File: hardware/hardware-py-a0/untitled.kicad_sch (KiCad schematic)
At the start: 25 parts, among them J12 Micro_SD_Card_Det2, J4 LCD_socket, J9 AudioJack4, Q8 BSS138, Q9 BSS138

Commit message: [dev] py-a0 board files
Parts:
- removed R13: 10k, Resistor_SMD:R_0805_2012Metric_Pad1.20x1.40mm_HandSolder, symbol Device:R
- R27: value 10k -> 1M
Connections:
- net BUZZER: now also Q8.1 (G), R27.1
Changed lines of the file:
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@@
+	)
+	(junction
+		(at 128.27 176.53)
+		(diameter 0)
+		(color 0 0 0 0)
 	)
 	(junction
@@
 	)
 	(junction
-		(at 128.27 176.53)
-		(diameter 0)
-		(color 0 0 0 0)
-	)
-	(junction
 		(at 91.44 67.31)
 		(diameter 0)
@@
 	(wire
 		(pts
+			(xy 128.27 176.53) (xy 158.75 176.53)
+		)
+		(stroke
+			(width 0)
+			(type default)
+		)
+	)
+	(wire
+		(pts
 			(xy 144.78 54.61) (xy 147.32 54.61)
 		)
@@
 		(pts
 			(xy 165.1 67.31) (xy 149.86 67.31)
-		)
-		(stroke
-			(width 0)
-			(type default)
-		)
-	)
-	(wire
-		(pts
-			(xy 135.89 176.53) (xy 158.75 176.53)
 		)
 		(stroke
@@
 			)
 		)
-		(property "Value" "10k"
+		(property "Value" "1M"
 			(at 125.476 180.848 90)
 			(effects
@@
 					(unit 1)
 				)
-			)
-		)
-	)
-	(symbol
-		(lib_id "Device:R")
-		(at 132.08 176.53 270)
-		(mirror x)
-		(unit 1)
-		(exclude_from_sim no)
-		(in_bom yes)
-		(on_board yes)
-		(dnp no)
-		(property "Reference" "R13"
-			(at 131.572 179.324 90)
-			(effects
-				(font
-					(size 1.27 1.27)
-				)
-			)
-		)
-		(property "Value" "10k"
-			(at 131.572 173.736 90)
-			(effects
-				(font
-					(size 1.27 1.27)
-				)
-			)
-		)
-		(property "Footprint" "Resistor_SMD:R_0805_2012Metric_Pad1.20x1.40mm_HandSolder"
-			(at 132.08 178.308 90)
-			(effects
-				(font
-					(size 1.27 1.27)
-				)
-				(hide yes)
-			)
-		)
-		(property "Datasheet" "~"
-			(at 132.08 176.53 0)
-			(effects
-				(font
-					(size 1.27 1.27)
-				)
-				(hide yes)
-			)
-		)
-		(property "Description" "Resistor"
-			(at 132.08 176.53 0)
-			(effects
-				(font
-					(size 1.27 1.27)
-				)
-				(hide yes)
-			)
-		)
-		(pin "1"
-		)
-		(pin "2"
-		)
-		(instances
-			(project "numcalcium"
-				(path "/842c0813-91d3-4f68-bc1f-ac3ce07be478/88d65574-4a55-44b9-b6d2-8e7d5a1c096b"
-					(reference "R13")
-					(unit 1)
-				)

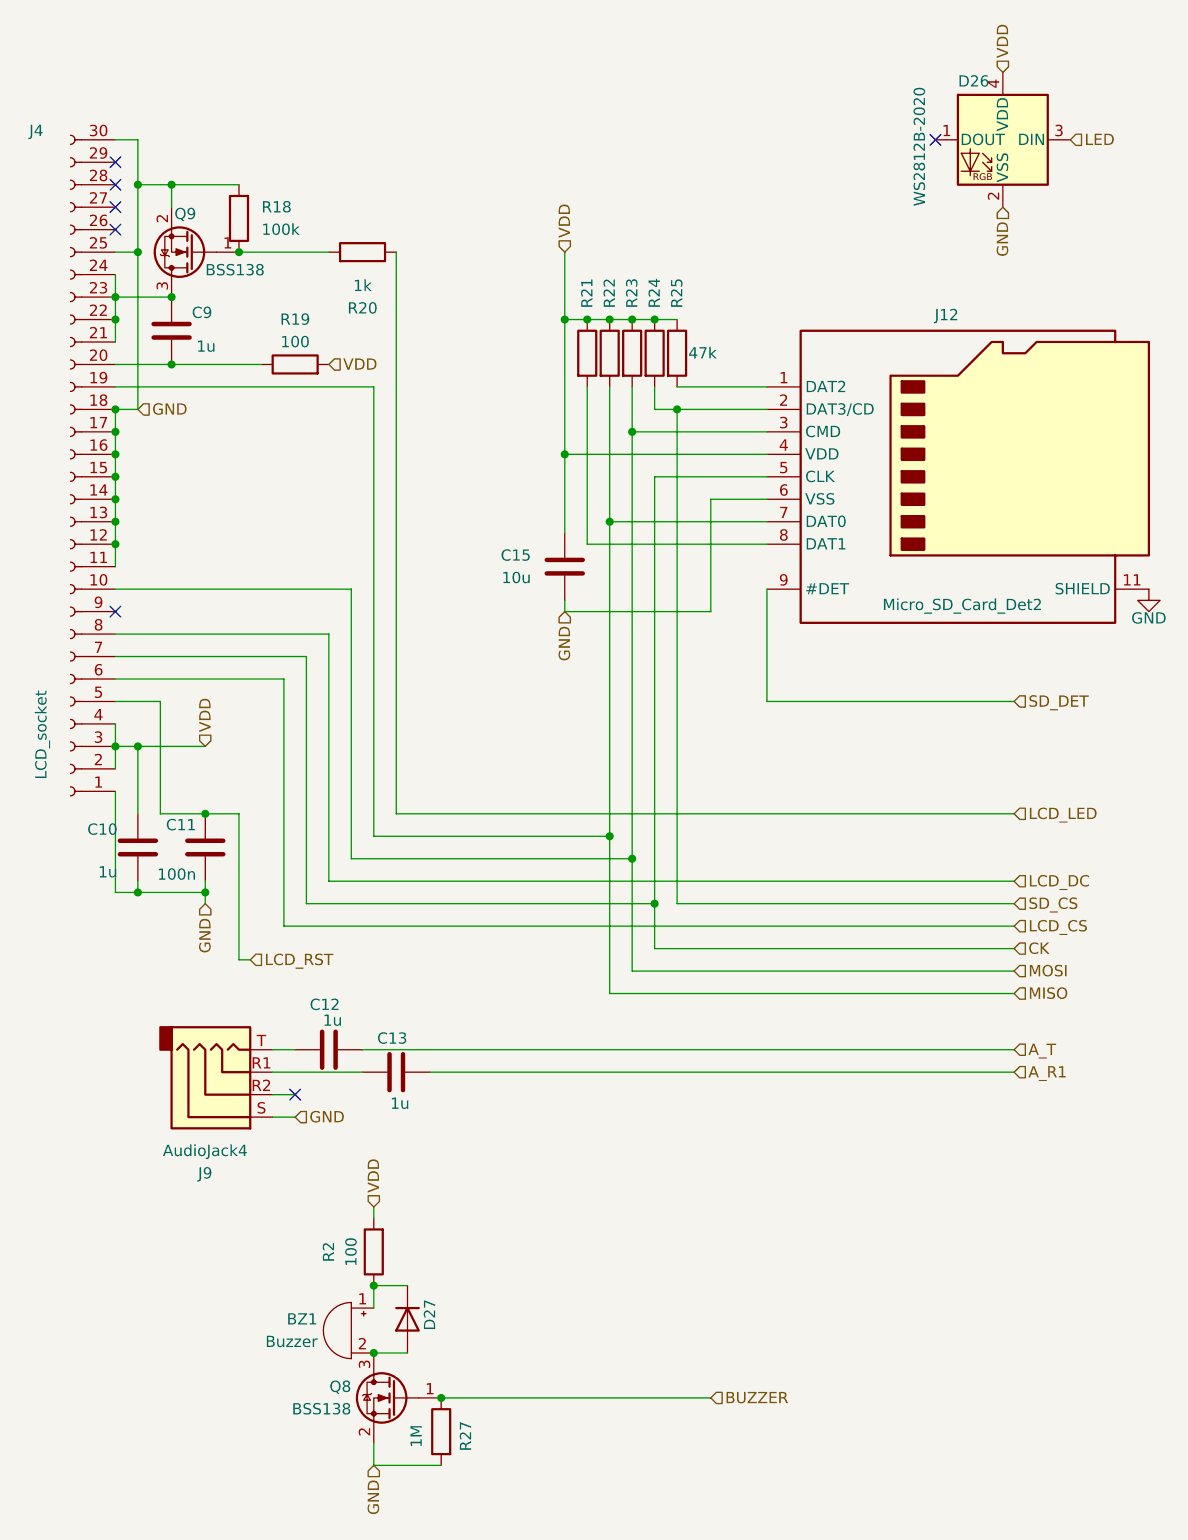
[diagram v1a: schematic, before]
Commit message: hardware: py/a0 revision 1.1 using FFC connectors
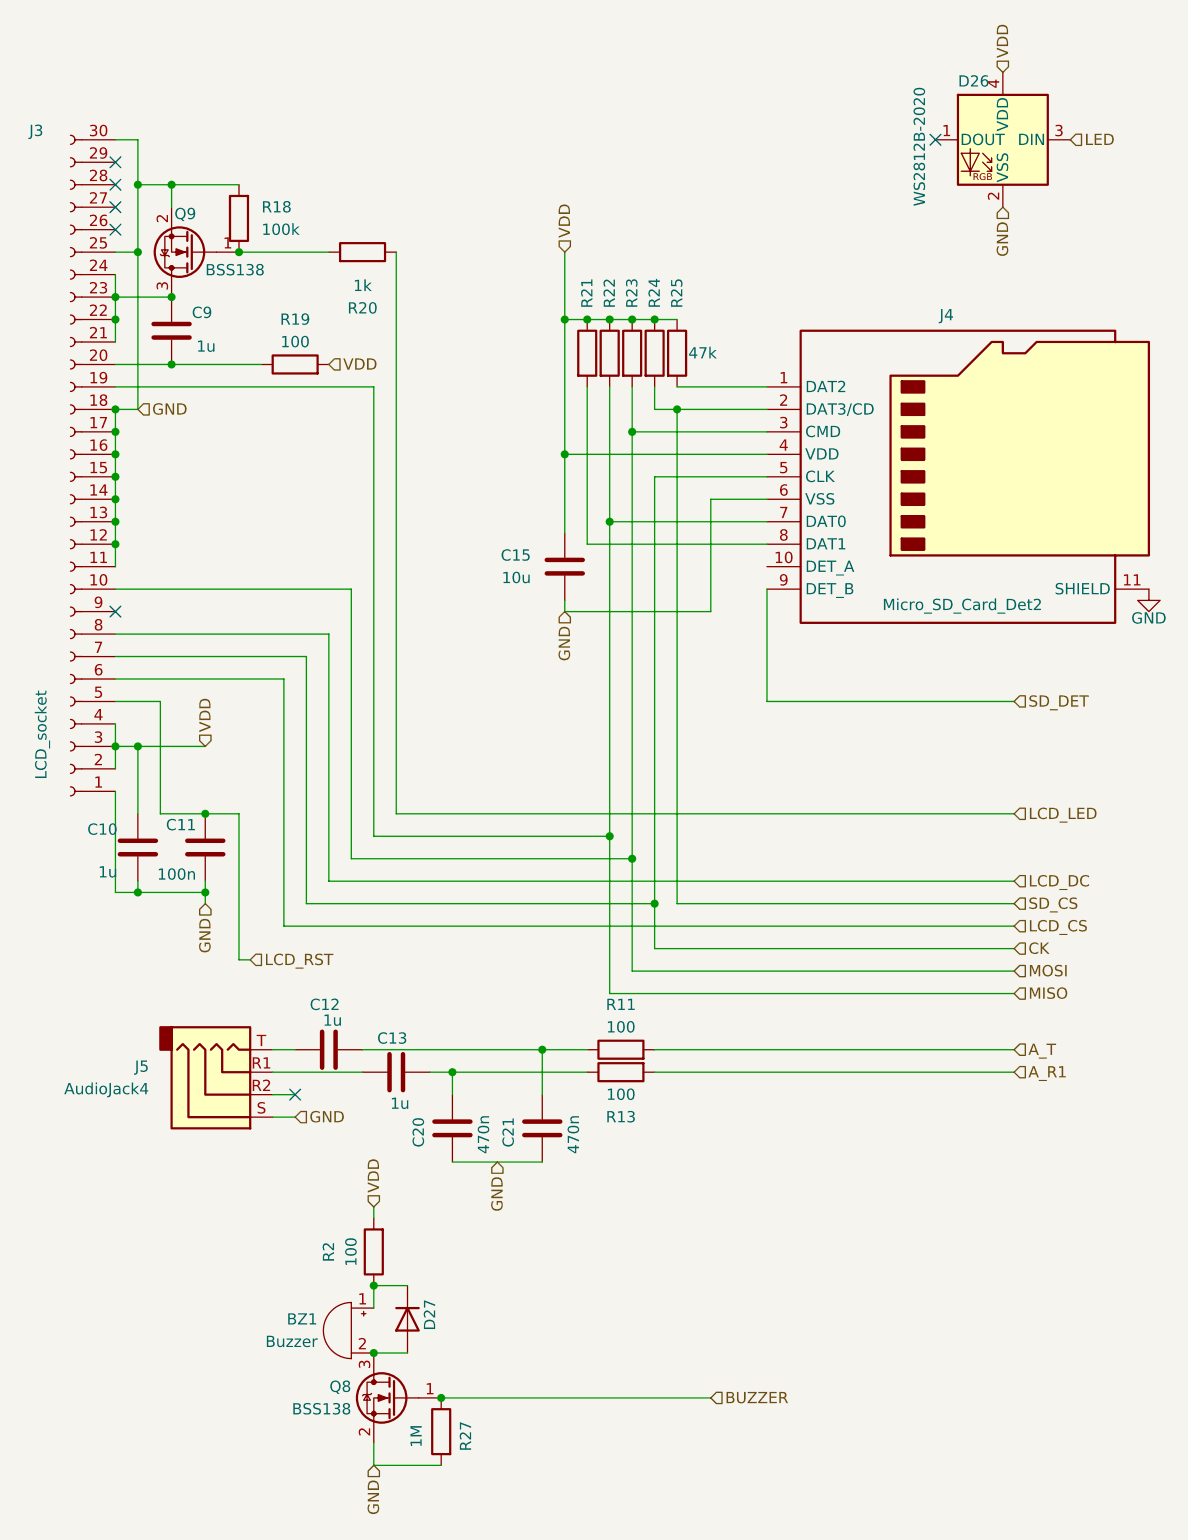
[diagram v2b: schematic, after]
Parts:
- added C20, C21: 470n, Capacitor_SMD:C_0805_2012Metric, symbol Device:C
- added R11, R13: 100, Resistor_SMD:R_0805_2012Metric_Pad1.20x1.40mm_HandSolder, symbol Device:R
- D27: footprint Diode_SMD:D_0805_2012Metric_Pad1.15x1.40mm_HandSolder -> Diode_SMD:D_1206_3216Metric
- renumbered J4 to J3, J12 to J4, J9 to J5
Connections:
- net A_R1: now also R13.2; no longer C13.2
- net A_T: now also R11.2; no longer C12.2
- net GND: now also C20.1, C21.1
- new net: C13.2, C20.2, R13.1
- new net: C12.2, C21.2, R11.1
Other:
- company, title: (none) -> MOTIV.PW

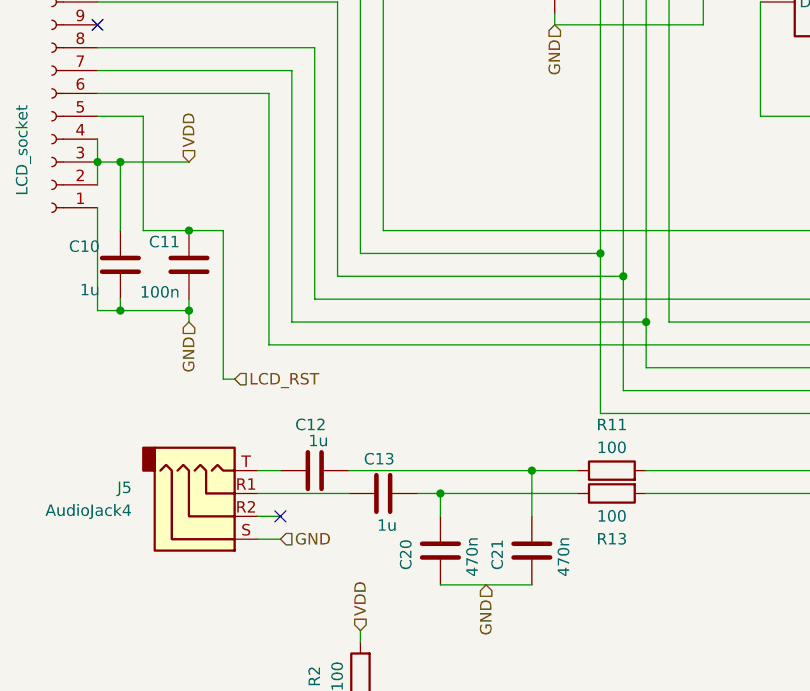
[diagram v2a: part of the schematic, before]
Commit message: terminal:os.dupterm Stream support
move files and rename folders to board_src and scripts
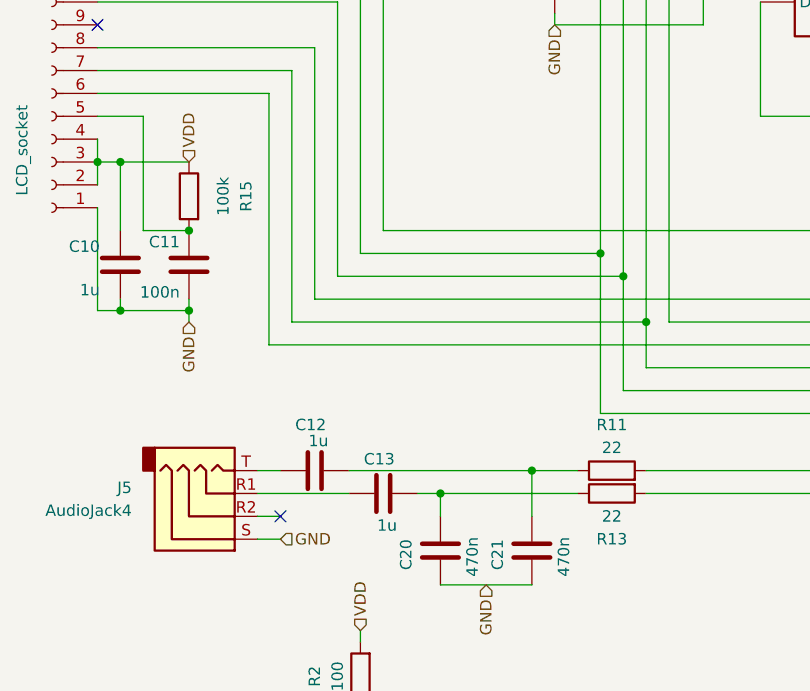
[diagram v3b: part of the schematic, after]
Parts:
- added R15: 100k, Resistor_SMD:R_0805_2012Metric_Pad1.20x1.40mm_HandSolder, symbol Device:R
- R11, R13: value 100 -> 22
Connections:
- net VDD: now also R15.1
- net LCD_RST: no longer names the net of C11.1, J3.5 (Pin_5)
- net LCD_RST: now also R15.2
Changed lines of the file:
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@@
+	)
+	(junction
+		(at 91.44 64.77)
+		(diameter 0)
+		(color 0 0 0 0)
+	)
+	(junction
+		(at 91.44 52.07)
+		(diameter 0)
+		(color 0 0 0 0)
+	)
+	(junction
+		(at 91.44 69.85)
+		(diameter 0)
+		(color 0 0 0 0)
+	)
+	(junction
+		(at 149.86 67.31)
+		(diameter 0)
+		(color 0 0 0 0)
+	)
+	(junction
+		(at 91.44 67.31)
+		(diameter 0)
+		(color 0 0 0 0)
+	)
+	(junction
+		(at 142.24 54.61)
+		(diameter 0)
+		(color 0 0 0 0)
+	)
+	(junction
+		(at 93.98 46.99)
+		(diameter 0)
+		(color 0 0 0 0)
+	)
+	(junction
+		(at 97.79 52.07)
+		(diameter 0)
+		(color 0 0 0 0)
+	)
+	(junction
+		(at 152.4 54.61)
+		(diameter 0)
+		(color 0 0 0 0)
+	)
+	(junction
+		(at 147.32 77.47)
+		(diameter 0)
+		(color 0 0 0 0)
+	)
+	(junction
+		(at 149.86 115.57)
+		(diameter 0)
+		(color 0 0 0 0)
+	)
+	(junction
+		(at 142.24 69.85)
+		(diameter 0)
+		(color 0 0 0 0)
+	)
+	(junction
+		(at 91.44 77.47)
+		(diameter 0)
+		(color 0 0 0 0)
 	)
 	(junction
@@
 	)
 	(junction
-		(at 91.44 64.77)
-		(diameter 0)
-		(color 0 0 0 0)
-	)
-	(junction
-		(at 91.44 52.07)
-		(diameter 0)
-		(color 0 0 0 0)
-	)
-	(junction
-		(at 91.44 69.85)
-		(diameter 0)
-		(color 0 0 0 0)
-	)
-	(junction
-		(at 149.86 67.31)
-		(diameter 0)
-		(color 0 0 0 0)
-	)
-	(junction
-		(at 91.44 67.31)
-		(diameter 0)
-		(color 0 0 0 0)
-	)
-	(junction
-		(at 142.24 54.61)
-		(diameter 0)
-		(color 0 0 0 0)
-	)
-	(junction
-		(at 93.98 46.99)
-		(diameter 0)
-		(color 0 0 0 0)
-	)
-	(junction
-		(at 97.79 52.07)
-		(diameter 0)
-		(color 0 0 0 0)
-	)
-	(junction
-		(at 152.4 54.61)
-		(diameter 0)
-		(color 0 0 0 0)
-	)
-	(junction
-		(at 147.32 77.47)
-		(diameter 0)
-		(color 0 0 0 0)
-	)
-	(junction
-		(at 149.86 115.57)
-		(diameter 0)
-		(color 0 0 0 0)
-	)
-	(junction
-		(at 142.24 69.85)
-		(diameter 0)
-		(color 0 0 0 0)
-	)
-	(junction
-		(at 91.44 77.47)
-		(diameter 0)
-		(color 0 0 0 0)
-	)
-	(junction
 		(at 129.54 139.7)
 		(diameter 0)
@@
 	(wire
 		(pts
-			(xy 105.41 110.49) (xy 101.6 110.49)
-		)
-		(stroke
-			(width 0)
-			(type default)
-		)
-	)
-	(wire
-		(pts
-			(xy 105.41 127) (xy 105.41 110.49)
-		)
-		(stroke
-			(width 0)
-			(type default)
-		)
-	)
-	(wire
-		(pts
 			(xy 120.65 154.94) (xy 120.65 156.21)
 		)
@@
 	(wire
 		(pts
-			(xy 105.41 127) (xy 106.68 127)
-		)
-		(stroke
-			(width 0)
-			(type default)
-		)
-	)
-	(wire
-		(pts
 			(xy 149.86 67.31) (xy 149.86 62.23)
 		)
@@
 		(shape input)
 		(at 111.76 144.78 0)
-		(fields_autoplaced yes)
-		(effects
-			(font
-				(size 1.27 1.27)
-			)
-			(justify left)
-		)
-	)
-	(hierarchical_label "LCD_RST"
-		(shape input)
-		(at 106.68 127 0)
 		(fields_autoplaced yes)
 		(effects
@@
 				(path "/842c0813-91d3-4f68-bc1f-ac3ce07be478/88d65574-4a55-44b9-b6d2-8e7d5a1c096b"
 					(reference "R22")
+					(unit 1)
+				)
+			)
+		)
+	)
+	(symbol
+		(lib_id "Device:R")
+		(at 101.6 106.68 0)
+		(mirror y)
+		(unit 1)
+		(exclude_from_sim no)
+		(in_bom yes)
+		(on_board yes)
+		(dnp no)
+		(property "Reference" "R15"
+			(at 107.95 106.68 90)
+			(effects
+				(font
+					(size 1.27 1.27)
+				)
+			)
+		)
+		(property "Value" "100k"
+			(at 105.41 106.68 90)
+			(effects
+				(font
+					(size 1.27 1.27)
+				)
+			)
+		)
+		(property "Footprint" "Resistor_SMD:R_0805_2012Metric_Pad1.20x1.40mm_HandSolder"
+			(at 103.378 106.68 90)
+			(effects
+				(font
+					(size 1.27 1.27)
+				)
+				(hide yes)
+			)
+		)
+		(property "Datasheet" "~"
+			(at 101.6 106.68 0)
+			(effects
+				(font
+					(size 1.27 1.27)
+				)
+				(hide yes)
+			)
+		)
+		(property "Description" "Resistor"
+			(at 101.6 106.68 0)
+			(effects
+				(font
+					(size 1.27 1.27)
+				)
+				(hide yes)
+			)
+		)
+		(pin "1"
+		)
+		(pin "2"
+		)
+		(instances
+			(project "numcalcium"
+				(path "/842c0813-91d3-4f68-bc1f-ac3ce07be478/88d65574-4a55-44b9-b6d2-8e7d5a1c096b"
+					(reference "R15")
 					(unit 1)
 				)
@@
 			)
 		)
-		(property "Value" "100"
+		(property "Value" "22"
 			(at 148.59 142.24 90)
 			(effects
@@
 			)
 		)
-		(property "Value" "100"
+		(property "Value" "22"
 			(at 148.59 134.62 90)
 			(effects
